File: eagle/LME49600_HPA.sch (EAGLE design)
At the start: 43 parts, among them IC1 OPA2134P, IC2 OPA2134P, P1 POLYSWITCH, P2 POLYSWITCH

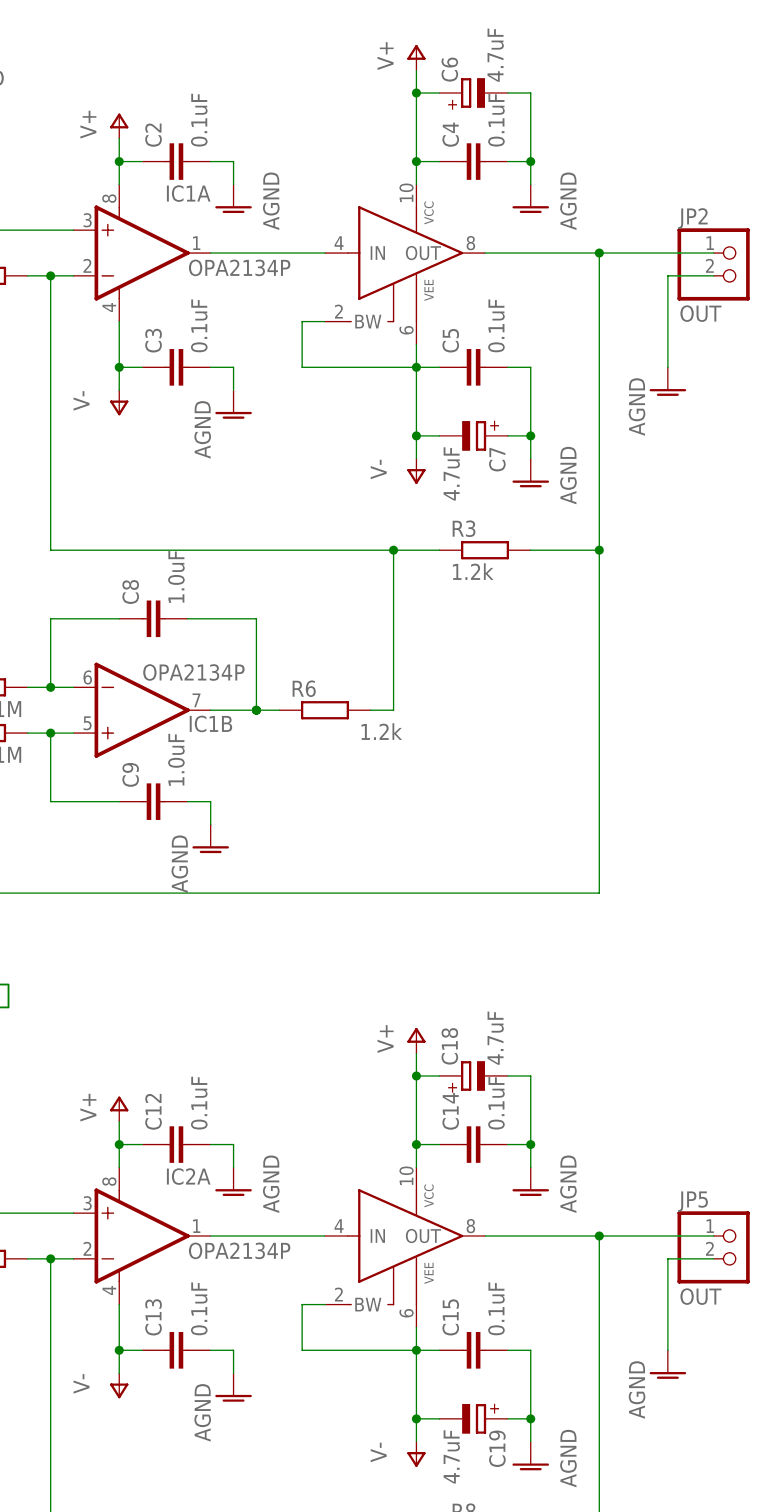
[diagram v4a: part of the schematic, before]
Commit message: Change board size of LME49600
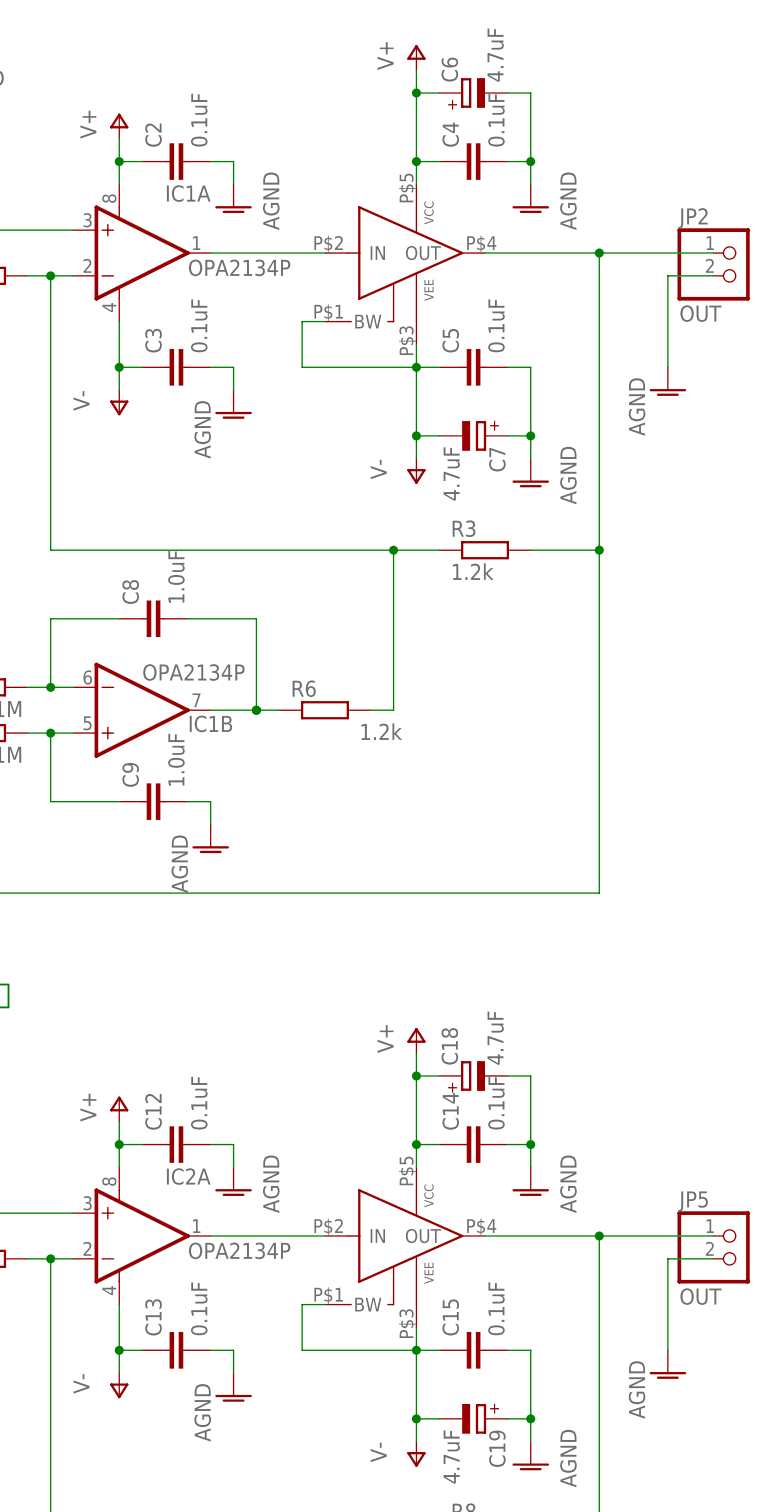
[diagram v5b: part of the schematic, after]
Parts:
- U$1, U$2: value LME49600_BRD -> LME49600-BRD2; device mylib2:LME49600_BRD -> mylib2:LME49600-BRD2
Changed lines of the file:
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@@
 <setting verticaltext="up"/>
 </settings>
-<grid distance="0.1" unitdist="inch" unit="inch" style="lines" multiple="1" display="yes" altdistance="0.01" altunitdist="inch" altunit="inch"/>
+<grid distance="0.1" unitdist="inch" unit="inch" style="lines" multiple="1" display="no" altdistance="0.01" altunitdist="inch" altunit="inch"/>
 <layers>
 <layer number="1" name="Top" color="4" fill="1" visible="no" active="no"/>
@@
 <part name="AGND5" library="supply1" deviceset="AGND" device=""/>
 <part name="R3" library="rcl" deviceset="R-EU_" device="0207/7" value="1.2k"/>
-<part name="U$1" library="mylib2" deviceset="LME49600_BRD" device=""/>
 <part name="P+1" library="supply1" deviceset="V+" device=""/>
 <part name="P-1" library="supply1" deviceset="V-" device=""/>
@@
 <part name="AGND16" library="supply1" deviceset="AGND" device=""/>
 <part name="R8" library="rcl" deviceset="R-EU_" device="0207/7" value="1.2k"/>
-<part name="U$2" library="mylib2" deviceset="LME49600_BRD" device=""/>
 <part name="P+4" library="supply1" deviceset="V+" device=""/>
 <part name="P-4" library="supply1" deviceset="V-" device=""/>
@@
 <part name="R12" library="rcl" deviceset="R-EU_" device="0207/7" value="1.2k"/>
 <part name="AGND23" library="supply1" deviceset="AGND" device=""/>
+<part name="U$1" library="mylib2" deviceset="LME49600-BRD2" device=""/>
+<part name="U$2" library="mylib2" deviceset="LME49600-BRD2" device=""/>
 </parts>
 <sheets>
@@
 <instance part="AGND5" gate="VR1" x="104.14" y="170.18"/>
 <instance part="R3" gate="G$1" x="132.08" y="154.94"/>
-<instance part="U$1" gate="G$1" x="121.92" y="187.96"/>
 <instance part="P+1" gate="1" x="124.46" y="210.82"/>
 <instance part="P-1" gate="1" x="124.46" y="162.56"/>
@@
 <instance part="AGND16" gate="VR1" x="104.14" y="60.96"/>
 <instance part="R8" gate="G$1" x="132.08" y="45.72"/>
-<instance part="U$2" gate="G$1" x="121.92" y="78.74"/>
 <instance part="P+4" gate="1" x="124.46" y="101.6"/>
 <instance part="P-4" gate="1" x="124.46" y="53.34"/>
@@
 <instance part="R12" gate="G$1" x="55.88" y="73.66" rot="R90"/>
 <instance part="AGND23" gate="VR1" x="55.88" y="63.5"/>
+<instance part="U$1" gate="G$1" x="121.92" y="187.96"/>
+<instance part="U$2" gate="G$1" x="121.92" y="78.74"/>
 </instances>
 <busses>
@@
 <segment>
 <pinref part="IC1" gate="A" pin="OUT"/>
+<wire x1="101.6" y1="187.96" x2="114.3" y2="187.96" width="0.1524" layer="91"/>
 <pinref part="U$1" gate="G$1" pin="IN"/>
-<wire x1="101.6" y1="187.96" x2="114.3" y2="187.96" width="0.1524" layer="91"/>
 </segment>
 </net>
 <net name="V-" class="0">
 <segment>
-<pinref part="U$1" gate="G$1" pin="BW"/>
 <wire x1="114.3" y1="180.34" x2="111.76" y2="180.34" width="0.1524" layer="91"/>
 <wire x1="111.76" y1="180.34" x2="111.76" y2="175.26" width="0.1524" layer="91"/>
 <wire x1="111.76" y1="175.26" x2="124.46" y2="175.26" width="0.1524" layer="91"/>
-<pinref part="U$1" gate="G$1" pin="VEE@1"/>
 <wire x1="124.46" y1="175.26" x2="124.46" y2="177.8" width="0.1524" layer="91"/>
 <pinref part="P-1" gate="1" pin="V-"/>
@@
 <junction x="124.46" y="167.64"/>
 <pinref part="C7" gate="G$1" pin="-"/>
+<pinref part="U$1" gate="G$1" pin="BW"/>
+<pinref part="U$1" gate="G$1" pin="VEE@1"/>
 </segment>
 <segment>
@@
 </segment>
 <segment>
-<pinref part="U$2" gate="G$1" pin="BW"/>
 <wire x1="114.3" y1="71.12" x2="111.76" y2="71.12" width="0.1524" layer="91"/>
 <wire x1="111.76" y1="71.12" x2="111.76" y2="66.04" width="0.1524" layer="91"/>
 <wire x1="111.76" y1="66.04" x2="124.46" y2="66.04" width="0.1524" layer="91"/>
-<pinref part="U$2" gate="G$1" pin="VEE@1"/>
 <wire x1="124.46" y1="66.04" x2="124.46" y2="68.58" width="0.1524" layer="91"/>
 <pinref part="P-4" gate="1" pin="V-"/>
@@
 <junction x="124.46" y="58.42"/>
 <pinref part="C19" gate="G$1" pin="-"/>
+<pinref part="U$2" gate="G$1" pin="BW"/>
+<pinref part="U$2" gate="G$1" pin="VEE@1"/>
 </segment>
 <segment>
@@
 <net name="V+" class="0">
 <segment>
-<pinref part="U$1" gate="G$1" pin="VCC"/>
 <pinref part="P+1" gate="1" pin="V+"/>
 <wire x1="124.46" y1="195.58" x2="124.46" y2="198.12" width="0.1524" layer="91"/>
@@
 <junction x="124.46" y="198.12"/>
 <pinref part="C6" gate="G$1" pin="+"/>
+<pinref part="U$1" gate="G$1" pin="VCC"/>
 </segment>
 <segment>
@@
 </segment>
 <segment>
-<pinref part="U$2" gate="G$1" pin="VCC"/>
 <pinref part="P+4" gate="1" pin="V+"/>
 <wire x1="124.46" y1="86.36" x2="124.46" y2="88.9" width="0.1524" layer="91"/>
@@
 <junction x="124.46" y="88.9"/>
 <pinref part="C18" gate="G$1" pin="+"/>
+<pinref part="U$2" gate="G$1" pin="VCC"/>
 </segment>
 <segment>
@@
 <segment>
 <pinref part="JP2" gate="G$1" pin="1"/>
-<pinref part="U$1" gate="G$1" pin="OUT"/>
 <wire x1="132.08" y1="187.96" x2="144.78" y2="187.96" width="0.1524" layer="91"/>
 <wire x1="144.78" y1="187.96" x2="157.48" y2="187.96" width="0.1524" layer="91"/>
@@
 <wire x1="68.58" y1="134.62" x2="68.58" y2="116.84" width="0.1524" layer="91"/>
 <wire x1="68.58" y1="116.84" x2="144.78" y2="116.84" width="0.1524" layer="91"/>
+<pinref part="U$1" gate="G$1" pin="OUT"/>
 </segment>
 </net>
@@
 <segment>
 <pinref part="IC2" gate="A" pin="OUT"/>
+<wire x1="101.6" y1="78.74" x2="114.3" y2="78.74" width="0.1524" layer="91"/>
 <pinref part="U$2" gate="G$1" pin="IN"/>
-<wire x1="101.6" y1="78.74" x2="114.3" y2="78.74" width="0.1524" layer="91"/>
 </segment>
 </net>
@@
 <segment>
 <pinref part="JP5" gate="G$1" pin="1"/>
-<pinref part="U$2" gate="G$1" pin="OUT"/>
 <wire x1="132.08" y1="78.74" x2="144.78" y2="78.74" width="0.1524" layer="91"/>
 <wire x1="144.78" y1="78.74" x2="157.48" y2="78.74" width="0.1524" layer="91"/>
@@
 <wire x1="68.58" y1="25.4" x2="68.58" y2="7.62" width="0.1524" layer="91"/>
 <wire x1="68.58" y1="7.62" x2="144.78" y2="7.62" width="0.1524" layer="91"/>
-</segment>
-</net>
+<pinref part="U$2" gate="G$1" pin="OUT"/>
+</segment>
+</net>

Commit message: Change: Board size of LME49600
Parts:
- C14, C15, C4, C5: device rcl:C-EU075-042X103 -> rcl:C-EU050H075X075
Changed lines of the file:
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@@
 <part name="P+1" library="supply1" deviceset="V+" device=""/>
 <part name="P-1" library="supply1" deviceset="V-" device=""/>
-<part name="C4" library="rcl" deviceset="C-EU" device="075-042X103" value="0.1uF"/>
-<part name="C5" library="rcl" deviceset="C-EU" device="075-042X103" value="0.1uF"/>
+<part name="C4" library="rcl" deviceset="C-EU" device="050H075X075" value="0.1uF"/>
+<part name="C5" library="rcl" deviceset="C-EU" device="050H075X075" value="0.1uF"/>
 <part name="AGND6" library="supply1" deviceset="AGND" device=""/>
 <part name="AGND7" library="supply1" deviceset="AGND" device=""/>
@@
 <part name="P+4" library="supply1" deviceset="V+" device=""/>
 <part name="P-4" library="supply1" deviceset="V-" device=""/>
-<part name="C14" library="rcl" deviceset="C-EU" device="075-042X103" value="0.1uF"/>
-<part name="C15" library="rcl" deviceset="C-EU" device="075-042X103" value="0.1uF"/>
+<part name="C14" library="rcl" deviceset="C-EU" device="050H075X075" value="0.1uF"/>
+<part name="C15" library="rcl" deviceset="C-EU" device="050H075X075" value="0.1uF"/>
 <part name="AGND17" library="supply1" deviceset="AGND" device=""/>
 <part name="AGND18" library="supply1" deviceset="AGND" device=""/>

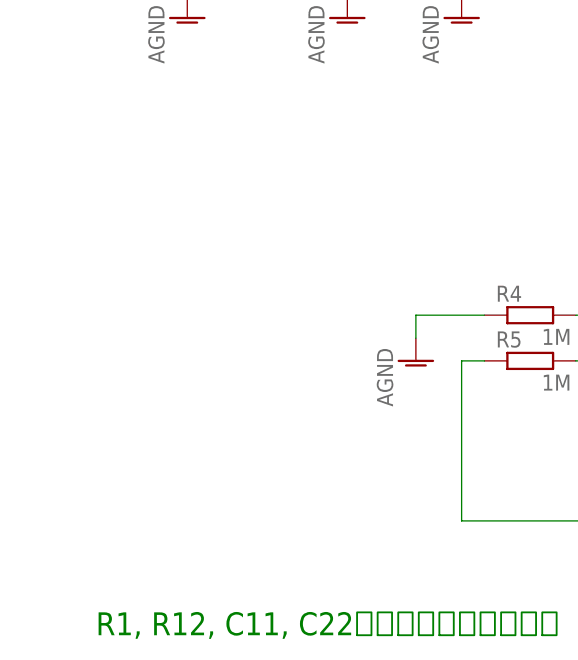
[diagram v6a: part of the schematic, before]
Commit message: Add: Pilot LED
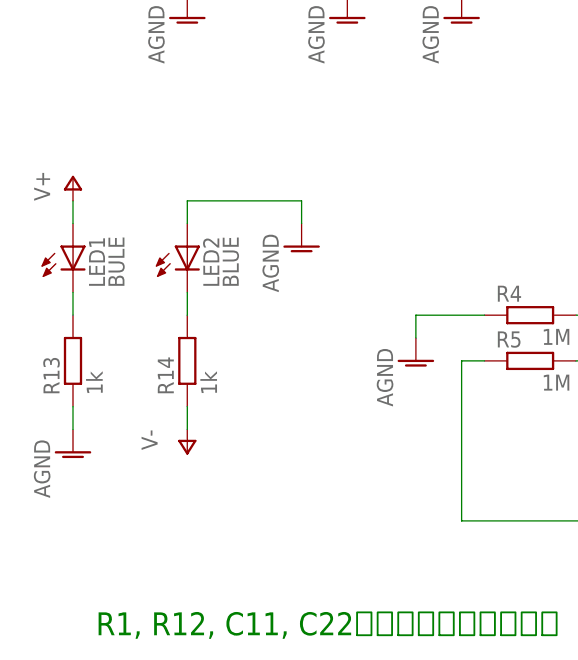
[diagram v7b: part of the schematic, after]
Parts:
- added LED1: BULE, led:LED3MM
- added LED2: BLUE, led:LED3MM
- added R13, R14: 1k, rcl:R-EU_0207/7
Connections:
- new net N$17: LED1.C, R13.2
- new net N$19: LED2.C, R14.2
- net AGND: now also LED2.A, R13.1
- net V+: now also LED1.A
- net V-: now also R14.1
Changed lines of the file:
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@@
 <setting verticaltext="up"/>
 </settings>
-<grid distance="0.1" unitdist="inch" unit="inch" style="lines" multiple="1" display="no" altdistance="0.01" altunitdist="inch" altunit="inch"/>
+<grid distance="0.1" unitdist="inch" unit="inch" style="lines" multiple="1" display="yes" altdistance="0.01" altunitdist="inch" altunit="inch"/>
 <layers>
 <layer number="1" name="Top" color="4" fill="1" visible="no" active="no"/>
@@
 <part name="U$1" library="mylib2" deviceset="LME49600-BRD2" device=""/>
 <part name="U$2" library="mylib2" deviceset="LME49600-BRD2" device=""/>
+<part name="LED1" library="led" deviceset="LED" device="3MM" value="BULE"/>
+<part name="LED2" library="led" deviceset="LED" device="3MM" value="BLUE"/>
+<part name="R13" library="rcl" deviceset="R-EU_" device="0207/7" value="1k"/>
+<part name="R14" library="rcl" deviceset="R-EU_" device="0207/7" value="1k"/>
+<part name="AGND10" library="supply1" deviceset="AGND" device=""/>
+<part name="AGND21" library="supply1" deviceset="AGND" device=""/>
+<part name="P+6" library="supply1" deviceset="V+" device=""/>
+<part name="P-6" library="supply1" deviceset="V-" device=""/>
 </parts>
 <sheets>
@@
 <instance part="U$1" gate="G$1" x="121.92" y="187.96"/>
 <instance part="U$2" gate="G$1" x="121.92" y="78.74"/>
+<instance part="LED1" gate="G$1" x="25.4" y="147.32"/>
+<instance part="LED2" gate="G$1" x="38.1" y="147.32"/>
+<instance part="R13" gate="G$1" x="25.4" y="134.62" rot="R90"/>
+<instance part="R14" gate="G$1" x="38.1" y="134.62" rot="R90"/>
+<instance part="AGND10" gate="VR1" x="25.4" y="124.46"/>
+<instance part="AGND21" gate="VR1" x="50.8" y="147.32"/>
+<instance part="P+6" gate="1" x="25.4" y="154.94"/>
+<instance part="P-6" gate="1" x="38.1" y="124.46"/>
 </instances>
 <busses>
@@
 <wire x1="55.88" y1="66.04" x2="55.88" y2="68.58" width="0.1524" layer="91"/>
 </segment>
+<segment>
+<pinref part="R13" gate="G$1" pin="1"/>
+<pinref part="AGND10" gate="VR1" pin="AGND"/>
+<wire x1="25.4" y1="129.54" x2="25.4" y2="127" width="0.1524" layer="91"/>
+</segment>
+<segment>
+<pinref part="LED2" gate="G$1" pin="A"/>
+<wire x1="38.1" y1="149.86" x2="38.1" y2="152.4" width="0.1524" layer="91"/>
+<wire x1="38.1" y1="152.4" x2="50.8" y2="152.4" width="0.1524" layer="91"/>
+<pinref part="AGND21" gate="VR1" pin="AGND"/>
+<wire x1="50.8" y1="152.4" x2="50.8" y2="149.86" width="0.1524" layer="91"/>
+</segment>
 </net>
 <net name="N$3" class="0">
@@
 <junction x="91.44" y="66.04"/>
 </segment>
+<segment>
+<pinref part="P-6" gate="1" pin="V-"/>
+<pinref part="R14" gate="G$1" pin="1"/>
+<wire x1="38.1" y1="127" x2="38.1" y2="129.54" width="0.1524" layer="91"/>
+</segment>
 </net>
 <net name="V+" class="0">
@@
 <wire x1="91.44" y1="91.44" x2="91.44" y2="88.9" width="0.1524" layer="91"/>
 <junction x="91.44" y="88.9"/>
+</segment>
+<segment>
+<pinref part="LED1" gate="G$1" pin="A"/>
+<pinref part="P+6" gate="1" pin="V+"/>
+<wire x1="25.4" y1="149.86" x2="25.4" y2="152.4" width="0.1524" layer="91"/>
 </segment>
 </net>
@@
 </segment>
 </net>
+<net name="N$17" class="0">
+<segment>
+<pinref part="R13" gate="G$1" pin="2"/>
+<pinref part="LED1" gate="G$1" pin="C"/>
+<wire x1="25.4" y1="139.7" x2="25.4" y2="142.24" width="0.1524" layer="91"/>
+</segment>
+</net>
+<net name="N$19" class="0">
+<segment>
+<pinref part="R14" gate="G$1" pin="2"/>
+<pinref part="LED2" gate="G$1" pin="C"/>
+<wire x1="38.1" y1="139.7" x2="38.1" y2="142.24" width="0.1524" layer="91"/>
+</segment>
+</net>

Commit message: Update: Board design
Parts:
- C11, C20: value (none) -> 2.2uF
- R1, R12: value 1.2k -> 47k
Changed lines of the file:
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@@
 <setting verticaltext="up"/>
 </settings>
-<grid distance="0.1" unitdist="inch" unit="inch" style="lines" multiple="1" display="yes" altdistance="0.01" altunitdist="inch" altunit="inch"/>
+<grid distance="0.1" unitdist="inch" unit="inch" style="lines" multiple="1" display="no" altdistance="0.01" altunitdist="inch" altunit="inch"/>
 <layers>
 <layer number="1" name="Top" color="4" fill="1" visible="no" active="no"/>
@@
 <part name="C6" library="rcl" deviceset="CPOL-EU" device="E2-4" value="4.7uF"/>
 <part name="C7" library="rcl" deviceset="CPOL-EU" device="E2-4" value="4.7uF"/>
-<part name="C11" library="rcl" deviceset="C-EU" device="050-055X075"/>
-<part name="R1" library="rcl" deviceset="R-EU_" device="0207/7" value="1.2k"/>
+<part name="C11" library="rcl" deviceset="C-EU" device="050-055X075" value="2.2uF"/>
+<part name="R1" library="rcl" deviceset="R-EU_" device="0207/7" value="47k"/>
 <part name="AGND12" library="supply1" deviceset="AGND" device=""/>
 <part name="JP4" library="pinhead" deviceset="PINHD-1X2" device="" value="IN"/>
@@
 <part name="C18" library="rcl" deviceset="CPOL-EU" device="E2-4" value="4.7uF"/>
 <part name="C19" library="rcl" deviceset="CPOL-EU" device="E2-4" value="4.7uF"/>
-<part name="C20" library="rcl" deviceset="C-EU" device="050-055X075"/>
-<part name="R12" library="rcl" deviceset="R-EU_" device="0207/7" value="1.2k"/>
+<part name="C20" library="rcl" deviceset="C-EU" device="050-055X075" value="2.2uF"/>
+<part name="R12" library="rcl" deviceset="R-EU_" device="0207/7" value="47k"/>
 <part name="AGND23" library="supply1" deviceset="AGND" device=""/>
 <part name="U$1" library="mylib2" deviceset="LME49600-BRD2" device=""/>
